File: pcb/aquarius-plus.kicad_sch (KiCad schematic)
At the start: 216 parts, among them J1 Cassette in, J10 Audio out, J11 Hand controller 2, J12 ESP USB Host, J13 Power in, J14 FPGA spare, J15 Expansion port, J16 ESP32 spare, J2 Cassette out, J3 SD_Card, J4 Printer, J5 Hand controller 1, J6 VGA, J7 DBG, J8 USB_A, J9 USB_A, Q1 BC847C, Q2 BC847C, SW1 SW_DPDT_x2, U1 XC3S200-4TQG144, U10 IS61C5128AS-25QLI, U11 74LVC4245APW, U12 74HC166, U13 SST39SF020A-55-4C-WHE, U14 74LVC4245APW, U15 LDL1117S33R, U16 MCP1700T-2502E/TT, U17 LD1117S12, U2 SN74CBTD3861PWR, U3 MAX3221ECPWR, U4 SN74CBTD3861PWR, U5 ESP32-S2-SOLO-N4R2, U6 SN74CBTD3861PWR, U7 Z84C0010AEG, U8 SN74CBTD3861PWR, U9 74HC166, X1 SG-5032CAN, X2 SG-5032CAN

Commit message: Bill of materials, schematic and gerber files.
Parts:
- J3: value SD_Card -> (none); footprint Connector_Card:SD_TE_2041021 -> (none)
- X1, X2: value SG-5032CAN -> (none)
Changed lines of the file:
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@@
   (title_block
     (title "Aquarius+")
-    (date "2022-04-01")
+    (date "2022-04-09")
     (rev "0")
     (company "Designed by Frank van den Hoef")
@@
     (in_bom yes) (on_board yes) (fields_autoplaced)
     (property "Reference" "J3" (id 0) (at 163.83 97.79 0))
-    (property "Value" "SD_Card" (id 1) (at 163.83 100.33 0))
-    (property "Footprint" "Connector_Card:SD_TE_2041021" (id 2) (at 163.83 115.57 0)
+    (property "Value" "" (id 1) (at 163.83 100.33 0))
+    (property "Footprint" "" (id 2) (at 163.83 115.57 0)
       (effects (font (size 1.27 1.27)) hide)
     )
-    (property "Datasheet" "http://portal.fciconnect.com/Comergent//fci/drawing/10067847.pdf" (id 3) (at 163.83 115.57 0)
+    (property "Datasheet" "" (id 3) (at 163.83 115.57 0)
       (effects (font (size 1.27 1.27)) hide)
     )
@@
       (effects (font (size 1.27 1.27)) (justify left))
     )
-    (property "Value" "SG-5032CAN" (id 1) (at 129.54 24.13 0)
-      (effects (font (size 1.27 1.27)) (justify left))
+    (property "Value" "" (id 1) (at 129.54 24.13 0)
+      (effects (font (size 0.8 0.8)) (justify left))
     )
     (property "Footprint" "Oscillator:Oscillator_SMD_SeikoEpson_SG8002LB-4Pin_5.0x3.2mm" (id 2) (at 144.78 39.37 0)
@@
       (effects (font (size 1.27 1.27)) (justify left))
     )
-    (property "Value" "SG-5032CAN" (id 1) (at 129.54 59.69 0)
-      (effects (font (size 1.27 1.27)) (justify left))
+    (property "Value" "" (id 1) (at 129.54 59.69 0)
+      (effects (font (size 0.8 0.8)) (justify left))
     )
     (property "Footprint" "Oscillator:Oscillator_SMD_SeikoEpson_SG8002LB-4Pin_5.0x3.2mm" (id 2) (at 144.78 74.93 0)
@@
   (symbol (lib_id "power:GND") (at 367.03 248.92 0) (mirror y) (unit 1)
     (in_bom yes) (on_board yes)
-    (property "Reference" "#PWR?" (id 0) (at 367.03 255.27 0)
+    (property "Reference" "#PWR0179" (id 0) (at 367.03 255.27 0)
       (effects (font (size 1.27 1.27)) hide)
     )
@@
     )
     (path "/d570a76b-ebb0-4d7d-9564-6c977401c409"
-      (reference "#PWR?") (unit 1) (value "GND") (footprint "")
+      (reference "#PWR0179") (unit 1) (value "GND") (footprint "")
     )
     (path "/52d4c05f-c0de-4113-8daf-5e4446b453ca"
@@
     )
     (path "/27195a63-df1c-474d-85f9-9425ca47e06f"
-      (reference "J3") (unit 1) (value "SD_Card") (footprint "Connector_Card:SD_TE_2041021")
+      (reference "J3") (unit 1) (value "Amphenol GSD090012SEU") (footprint "Connector_Card:SD_TE_2041021")
     )
     (path "/00d40a96-635b-492d-b814-850e0ac5cd48"
@@
     )
     (path "/6f28241f-7fad-4843-bd2a-6687c81d0a93"
-      (reference "X1") (unit 1) (value "SG-5032CAN") (footprint "Oscillator:Oscillator_SMD_SeikoEpson_SG8002LB-4Pin_5.0x3.2mm")
+      (reference "X1") (unit 1) (value "ECS-5032MV-143-CN-TR") (footprint "Oscillator:Oscillator_SMD_SeikoEpson_SG8002LB-4Pin_5.0x3.2mm")
     )
     (path "/ab3e3c77-3545-4f15-ac37-7d36b438edad"
-      (reference "X2") (unit 1) (value "SG-5032CAN") (footprint "Oscillator:Oscillator_SMD_SeikoEpson_SG8002LB-4Pin_5.0x3.2mm")
+      (reference "X2") (unit 1) (value "ECS-5032MV-480-BN-TR") (footprint "Oscillator:Oscillator_SMD_SeikoEpson_SG8002LB-4Pin_5.0x3.2mm")
     )
   )

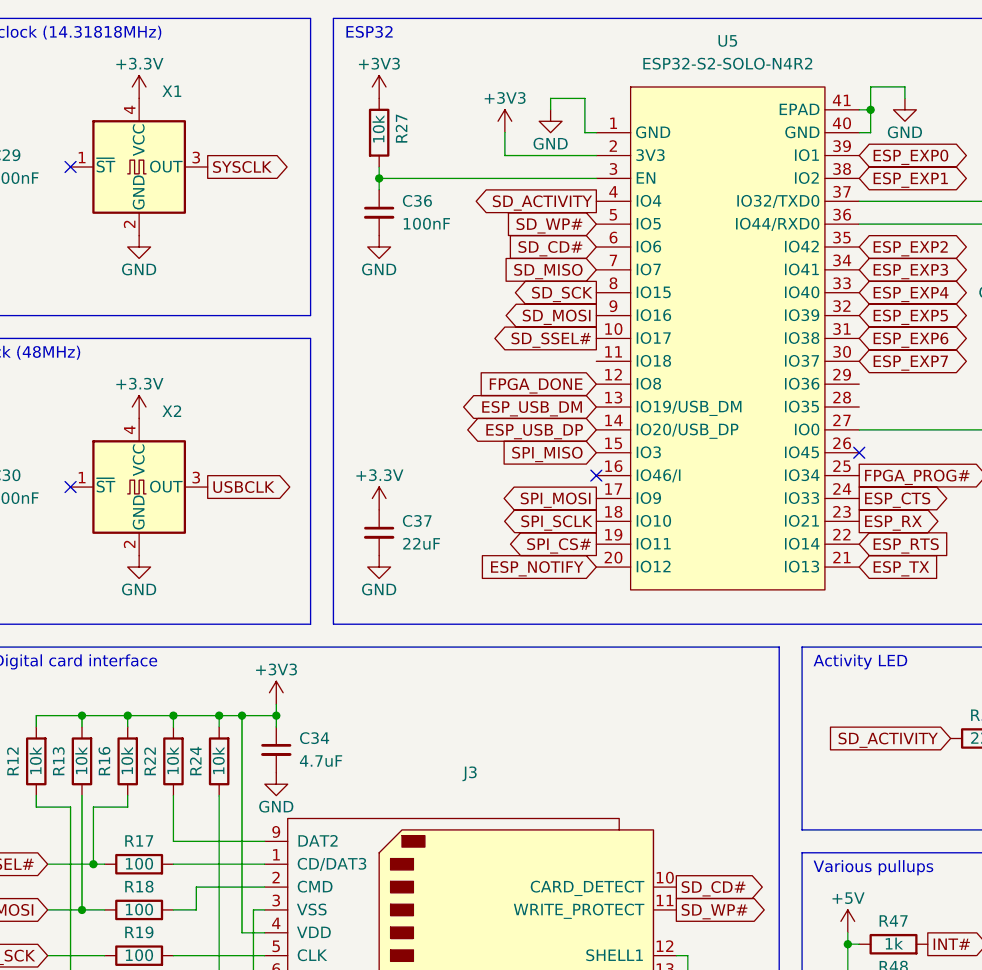
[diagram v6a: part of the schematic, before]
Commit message: ESP32 symbol fix.
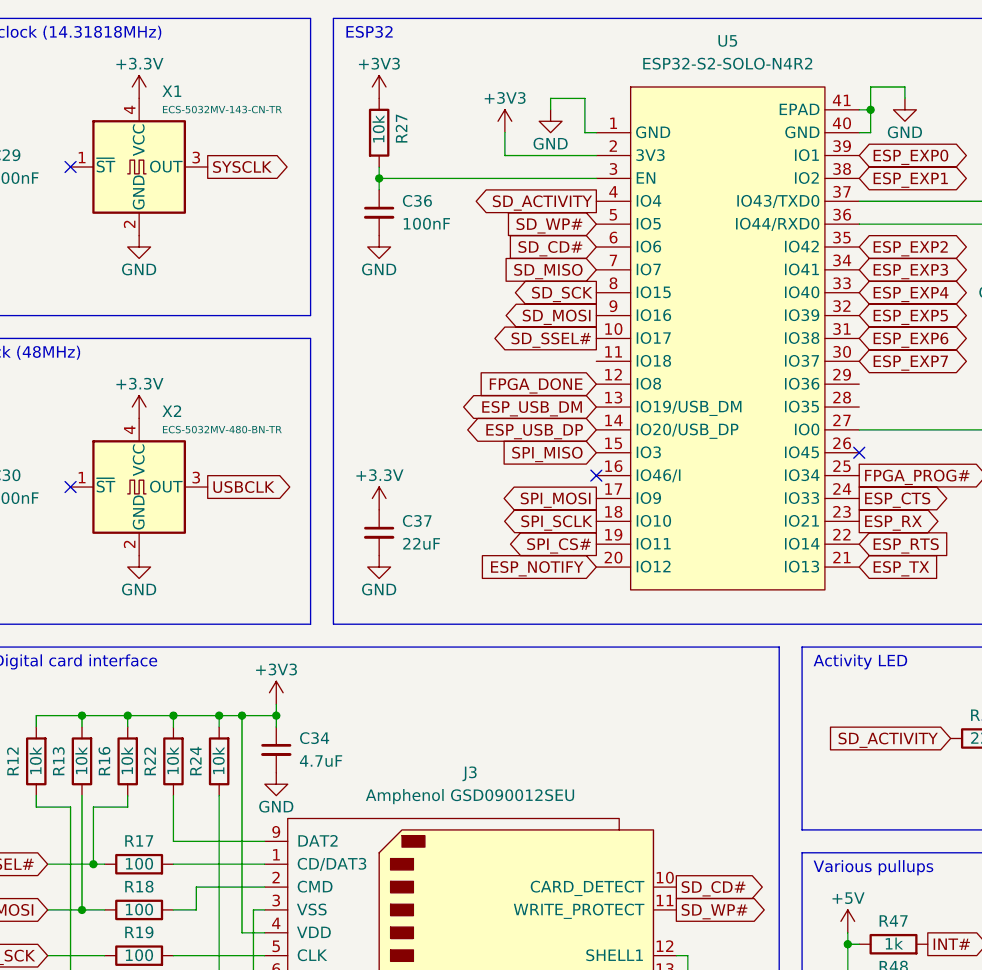
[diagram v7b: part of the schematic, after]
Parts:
- J3: value (none) -> Amphenol GSD090012SEU; footprint (none) -> Connector_Card:SD_TE_2041021
- X1: value (none) -> ECS-5032MV-143-CN-TR
- X2: value (none) -> ECS-5032MV-480-BN-TR
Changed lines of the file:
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@@
     (in_bom yes) (on_board yes) (fields_autoplaced)
     (property "Reference" "J3" (id 0) (at 163.83 97.79 0))
-    (property "Value" "" (id 1) (at 163.83 100.33 0))
-    (property "Footprint" "" (id 2) (at 163.83 115.57 0)
+    (property "Value" "Amphenol GSD090012SEU" (id 1) (at 163.83 100.33 0))
+    (property "Footprint" "Connector_Card:SD_TE_2041021" (id 2) (at 163.83 115.57 0)
       (effects (font (size 1.27 1.27)) hide)
     )
@@
       (effects (font (size 1.27 1.27)) (justify left))
     )
-    (property "Value" "" (id 1) (at 129.54 24.13 0)
+    (property "Value" "ECS-5032MV-143-CN-TR" (id 1) (at 129.54 24.13 0)
       (effects (font (size 0.8 0.8)) (justify left))
     )
@@
       (effects (font (size 1.27 1.27)) (justify left))
     )
-    (property "Value" "" (id 1) (at 129.54 59.69 0)
+    (property "Value" "ECS-5032MV-480-BN-TR" (id 1) (at 129.54 59.69 0)
       (effects (font (size 0.8 0.8)) (justify left))
     )
